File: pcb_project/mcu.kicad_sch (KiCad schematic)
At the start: 24 parts, among them J3 Conn_ST_STDC14, SW1 SW_SPST, SW2 SW_SPDT, U4 STM32U595VJTx, Y2 48MHz

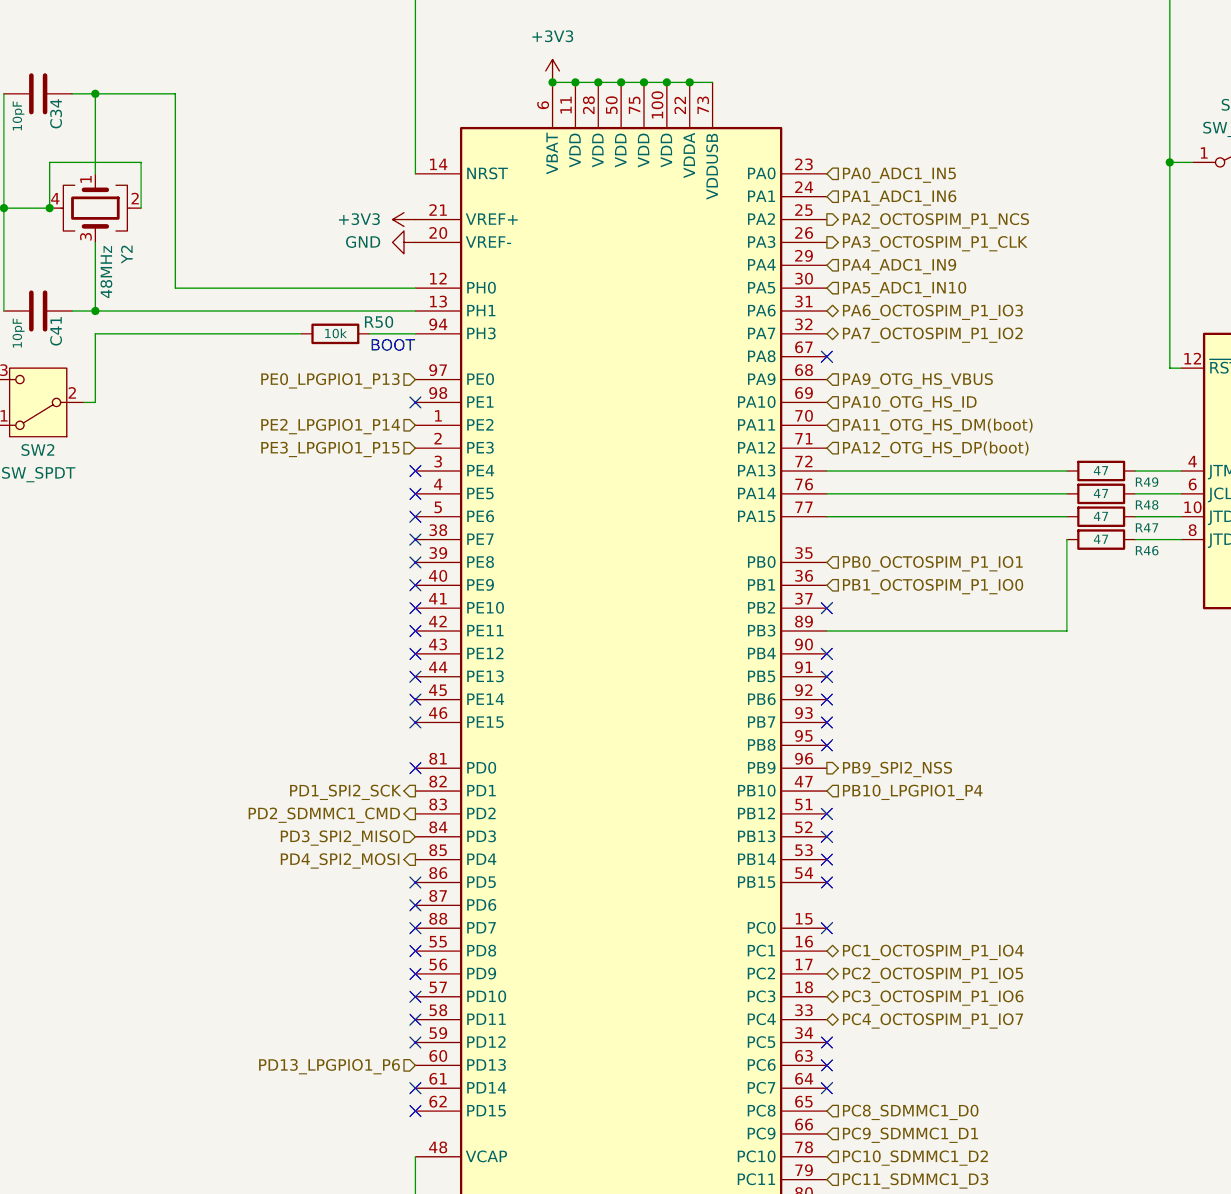
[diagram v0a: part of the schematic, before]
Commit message: Update USB component and redo pin choices for MCU
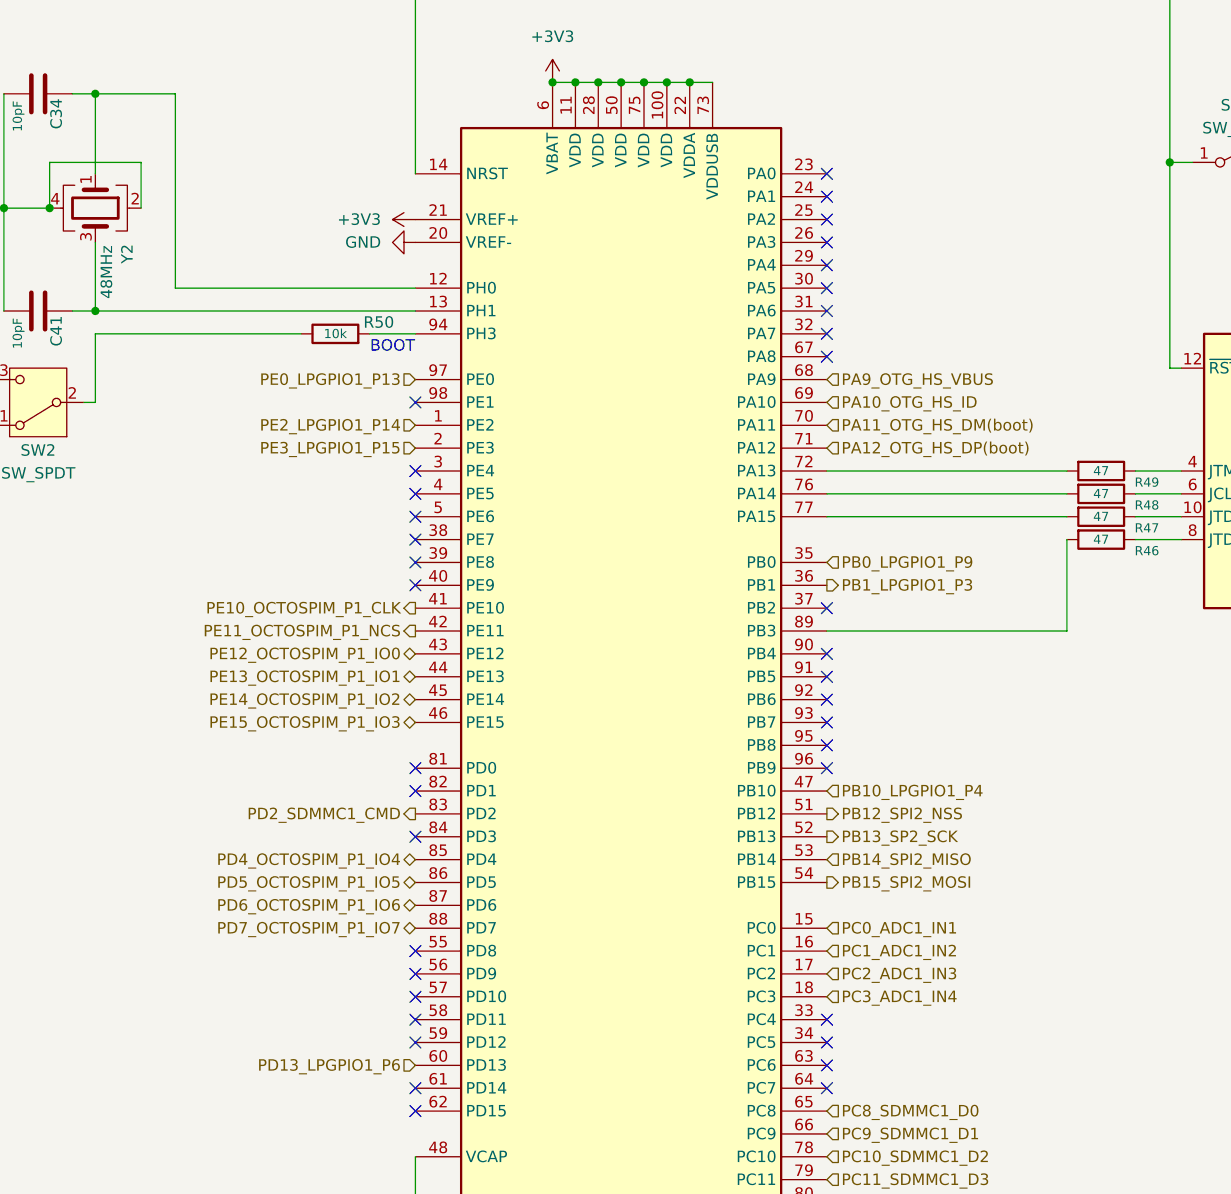
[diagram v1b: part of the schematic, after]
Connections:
- net PC0_ADC1_IN1: now reaches U4.15 (PC0)
- net PE10_OCTOSPIM_P1_CLK: now reaches U4.41 (PE10)
- net PE11_OCTOSPIM_P1_NCS: now reaches U4.42 (PE11)
- net PE12_OCTOSPIM_P1_IO0: now reaches U4.43 (PE12)
- net PE13_OCTOSPIM_P1_IO1: now reaches U4.44 (PE13)
- net PE14_OCTOSPIM_P1_IO2: now reaches U4.45 (PE14)
- net PE15_OCTOSPIM_P1_IO3: now reaches U4.46 (PE15)
- net PB12_SPI2_NSS: now reaches U4.51 (PB12)
- net PB13_SP2_SCK: now reaches U4.52 (PB13)
- net PB14_SPI2_MISO: now reaches U4.53 (PB14)
- net PB15_SPI2_MOSI: now reaches U4.54 (PB15)
- net PD5_OCTOSPIM_P1_IO5: now reaches U4.86 (PD5)
- net PD6_OCTOSPIM_P1_IO6: now reaches U4.87 (PD6)
- net PD7_OCTOSPIM_P1_IO7: now reaches U4.88 (PD7)
- net PA0_ADC1_IN5: no longer names the net of U4.23 (PA0)
- net PA1_ADC1_IN6: no longer names the net of U4.24 (PA1)
- net PA2_OCTOSPIM_P1_NCS: no longer names the net of U4.25 (PA2)
- net PA3_OCTOSPIM_P1_CLK: no longer names the net of U4.26 (PA3)
- net PA4_ADC1_IN9: no longer names the net of U4.29 (PA4)
- net PA5_ADC1_IN10: no longer names the net of U4.30 (PA5)
- net PA6_OCTOSPIM_P1_IO3: no longer names the net of U4.31 (PA6)
- net PA7_OCTOSPIM_P1_IO2: no longer names the net of U4.32 (PA7)
- net PB0_OCTOSPIM_P1_IO1 renamed PB0_LPGPIO1_P9
- net PB1_OCTOSPIM_P1_IO0 renamed PB1_LPGPIO1_P3
- net PB9_SPI2_NSS: no longer names the net of U4.96 (PB9)
- net PC1_OCTOSPIM_P1_IO4 renamed PC1_ADC1_IN2
- net PC2_OCTOSPIM_P1_IO5 renamed PC2_ADC1_IN3
- net PC3_OCTOSPIM_P1_IO6 renamed PC3_ADC1_IN4
- net PC4_OCTOSPIM_P1_IO7: no longer names the net of U4.33 (PC4)
- net PD1_SPI2_SCK: no longer names the net of U4.82 (PD1)
- net PD3_SPI2_MISO: no longer names the net of U4.84 (PD3)
- net PD4_SPI2_MOSI renamed PD4_OCTOSPIM_P1_IO4
- no-connect marks 46 -> 44

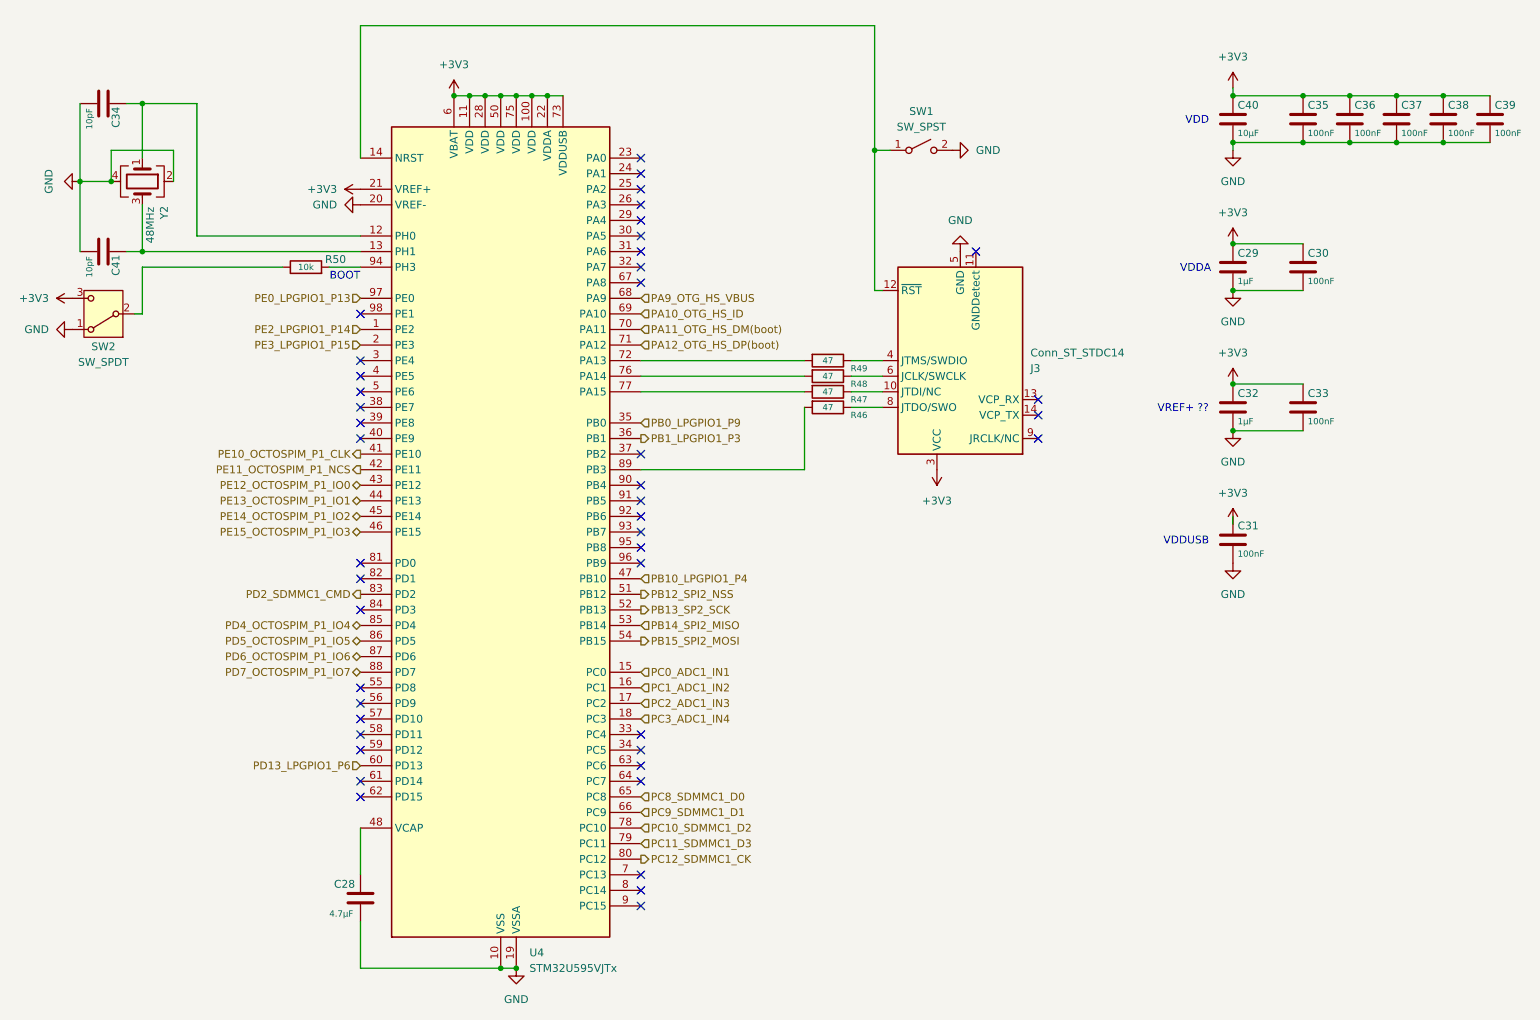
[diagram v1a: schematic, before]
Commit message: ERC fixes, some remain
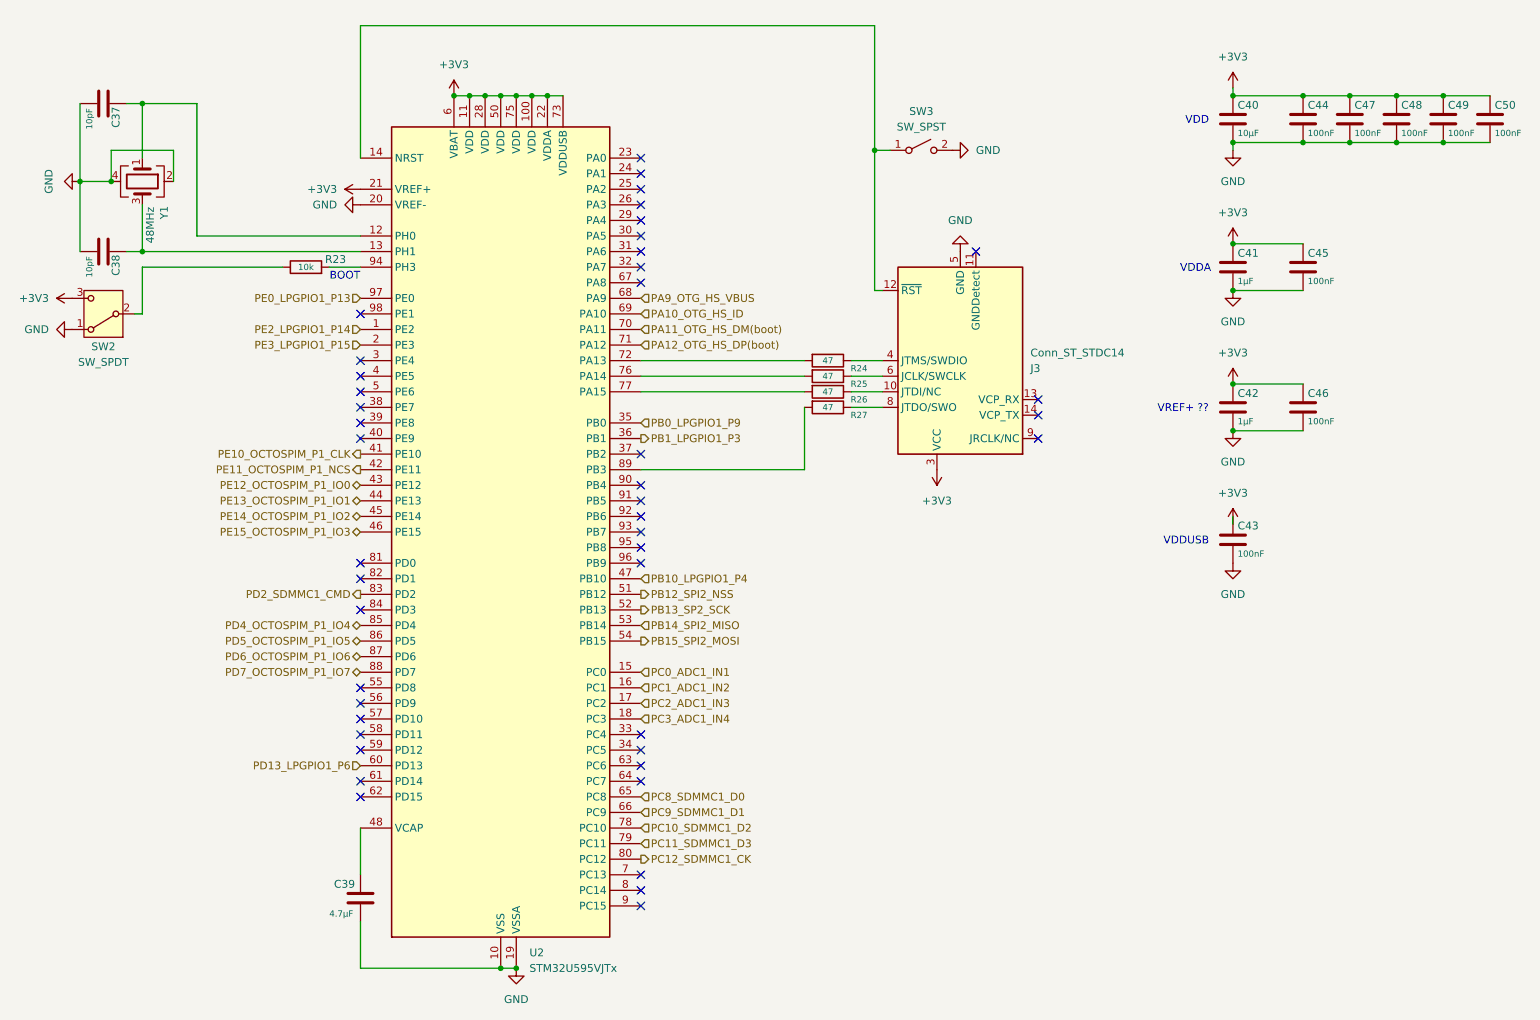
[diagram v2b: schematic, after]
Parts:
- renumbered C34 to C37, C41 to C38, C28 to C39, C29 to C41, C32 to C42, C31 to C43, C35 to C44, C30 to C45, C33 to C46, C36 to C47, C37 to C48, C38 to C49, C39 to C50, R50 to R23, R49 to R24, R48 to R25, R47 to R26, R46 to R27, SW1 to SW3, U4 to U2, Y2 to Y1

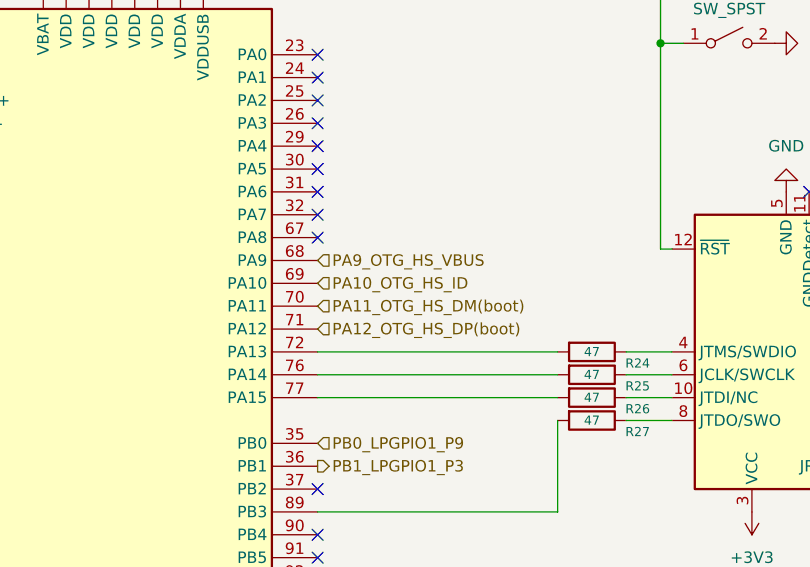
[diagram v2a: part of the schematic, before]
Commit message: Fix USB pins and other ERC errors
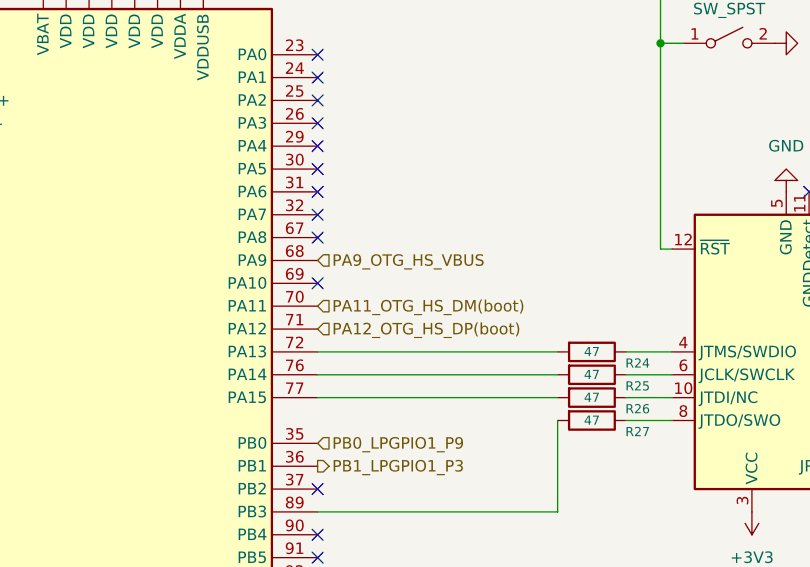
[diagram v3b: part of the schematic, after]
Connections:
- net PA10_OTG_HS_ID: no longer names the net of U2.69 (PA10)
- no-connect marks 44 -> 45
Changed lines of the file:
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@@
+	)
+	(no_connect
+		(at 124.46 64.77)
 	)
 	(no_connect
@@
 		(effects
 			(font
-				(size 1.27 1.27)
-			)
-			(justify left)
-		)
-	)
-	(hierarchical_label "PA10_OTG_HS_ID"
-		(shape input)
-		(at 124.46 64.77 0)
-		(effects
-			(font

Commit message: Fix JTAG connector, add pullups (FPGA has internal pullups as well), add some capacitor footprints
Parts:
- C43, C44, C45, C46, C47, C48, C49, C50: footprint (none) -> Capacitor_SMD:C_0603_1608Metric_Pad1.08x0.95mm_HandSolder
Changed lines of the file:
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@@
 			)
 		)
-		(property "Footprint" ""
+		(property "Footprint" "Capacitor_SMD:C_0603_1608Metric_Pad1.08x0.95mm_HandSolder"
 			(at 233.3752 36.83 0)
 			(effects
@@
 			)
 		)
-		(property "Footprint" ""
+		(property "Footprint" "Capacitor_SMD:C_0603_1608Metric_Pad1.08x0.95mm_HandSolder"
 			(at 263.8552 36.83 0)
 			(effects
@@
 			)
 		)
-		(property "Footprint" ""
+		(property "Footprint" "Capacitor_SMD:C_0603_1608Metric_Pad1.08x0.95mm_HandSolder"
 			(at 240.9952 36.83 0)
 			(effects
@@
 			)
 		)
-		(property "Footprint" ""
+		(property "Footprint" "Capacitor_SMD:C_0603_1608Metric_Pad1.08x0.95mm_HandSolder"
 			(at 256.2352 36.83 0)
 			(effects
@@
 			)
 		)
-		(property "Footprint" ""
+		(property "Footprint" "Capacitor_SMD:C_0603_1608Metric_Pad1.08x0.95mm_HandSolder"
 			(at 221.9452 105.41 0)
 			(effects
@@
 			)
 		)
-		(property "Footprint" ""
+		(property "Footprint" "Capacitor_SMD:C_0603_1608Metric_Pad1.08x0.95mm_HandSolder"
 			(at 248.6152 36.83 0)
 			(effects
@@
 			)
 		)
-		(property "Footprint" ""
+		(property "Footprint" "Capacitor_SMD:C_0603_1608Metric_Pad1.08x0.95mm_HandSolder"
 			(at 233.3752 60.96 0)
 			(effects
@@
 			)
 		)
-		(property "Footprint" ""
+		(property "Footprint" "Capacitor_SMD:C_0603_1608Metric_Pad1.08x0.95mm_HandSolder"
 			(at 233.3752 83.82 0)
 			(effects
